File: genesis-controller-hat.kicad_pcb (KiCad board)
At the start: 2 copper layers, 65 x 56 mm, 7 parts, among them J1 GPIO, J2 DSUB-9_Socket_Horizontal_P2.7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, J3 DSUB-9_Socket_Horizontal_P2.7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

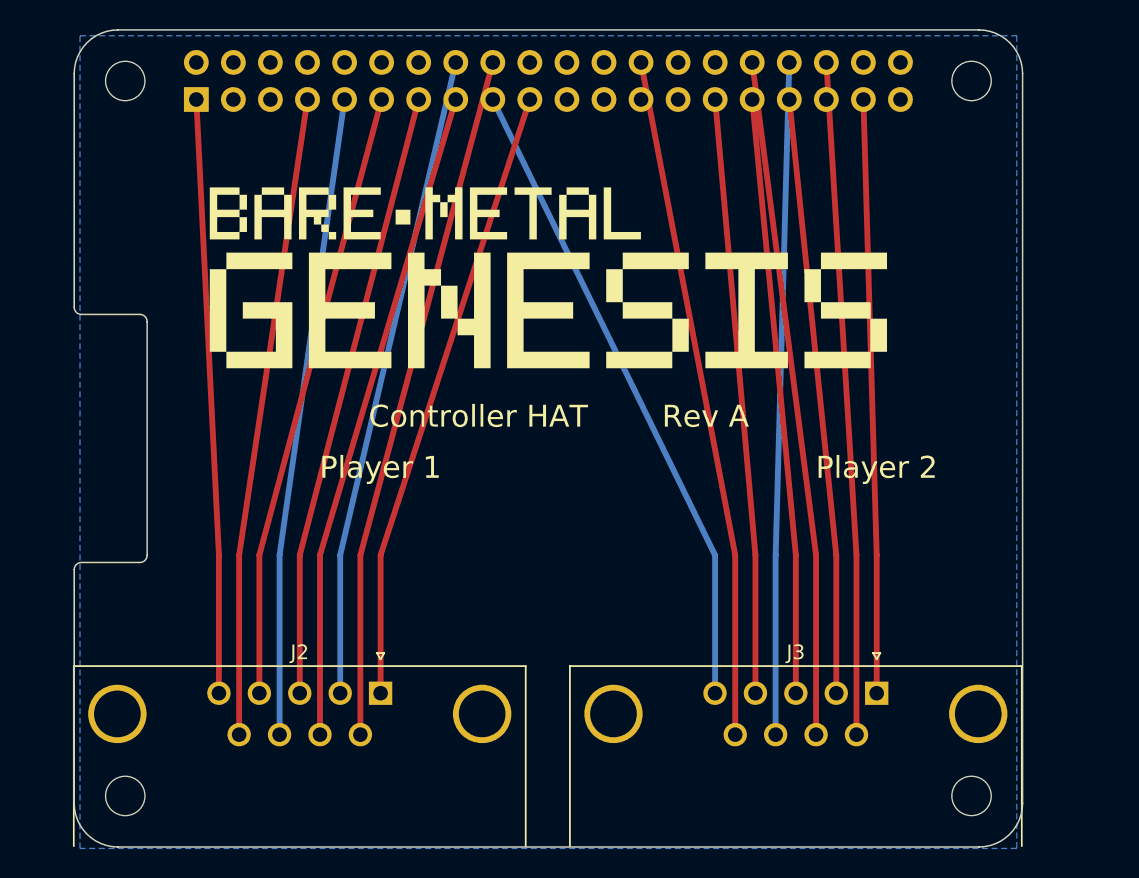
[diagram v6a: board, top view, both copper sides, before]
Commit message: Fix shorting_items and solder_mask_bridge by jogging tracks around J1's row-A pins
Root cause: J1's two pin rows are only 2.54mm apart. A track targeting a
row-B pin was routed as a straight diagonal that skimmed directly past the
row-A pin in the same column, since the diagonal has to pass through that
column's row-A position en route to row-B. Fixed by rerouting each affected
track (/GPIO24, /GPIO23, /GPIO7/SPI0.CE1, GND, /GPIO16, /GPIO12/PWM0) as:
breakout -> horizontal repositioning done entirely above J1's pin field
(y=60, clear of any pad) -> a pure-vertical run at a waypoint X exactly
between two header columns -> a short final hop into the target pad. Layer
assignment for all 12 signal nets + GND was then re-solved globally
(distance-based conflict check, not just literal intersection) to restore
zero same-layer crossings for the newly-shaped paths.

Result: shorting_items 7->0, solder_mask_bridge 6->0. Total DRC 17/5 -> 6/5.

Residual: 2 tracks_crossing remain (/GPIO12/PWM0 vs GND, /GPIO24 vs a
neighbor) in a cluster where 3+ nets mutually conflict -- more than 2
layers can pairwise-separate. This is a genuine topological limit of
2-layer routing in this specific column cluster, not a missed assignment;
resolving it needs a via or manual interactive routing, documented in
README.md as the remaining pre-fab cleanup item.

Co-Authored-By: Claude Sonnet 5 <noreply@anthropic.com>
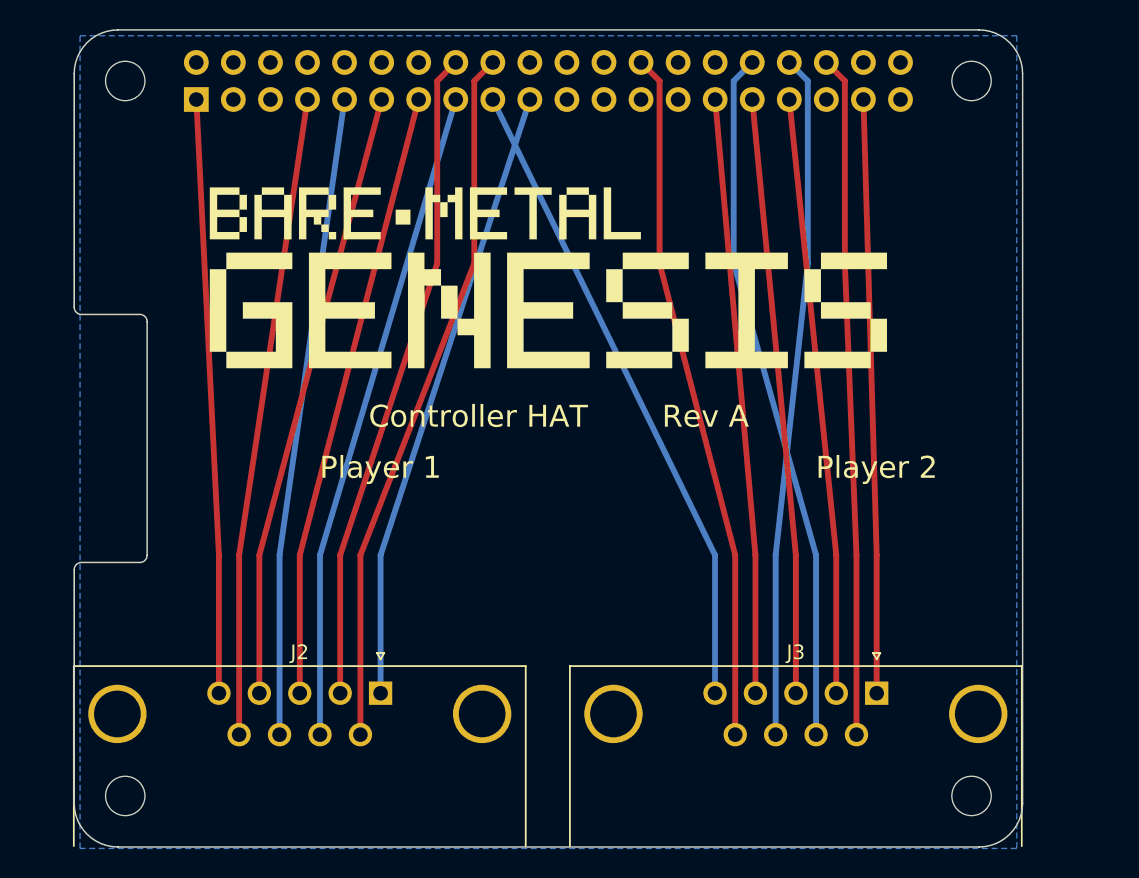
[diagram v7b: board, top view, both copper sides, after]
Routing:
- net /GPIO12/PWM0: track 46.4 -> 47.4 mm
- net /GPIO24: track 47.3 -> 48.1 mm
- net /GPIO23: track 44.1 -> 44.8 mm
- net GND: track 89.9 -> 90.6 mm
- net /GPIO7/SPI0.CE1: track 46.7 -> 47.3 mm
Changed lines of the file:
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@@
 	)
 	(segment
-		(start 153.615 80)
-		(end 151.55 46.23)
+		(start 152.82 60)
+		(end 152.82 47.5)
 		(width 0.4)
 		(layer "F.Cu")
@@
 	)
 	(segment
-		(start 150.845 80)
-		(end 146.47 46.23)
-		(width 0.4)
-		(layer "F.Cu")
+		(start 153.615 80)
+		(end 152.82 60)
+		(width 0.4)
+		(layer "F.Cu")
+		(net "/GPIO16")
+	)
+	(segment
+		(start 152.82 47.5)
+		(end 151.55 46.23)
+		(width 0.4)
+		(layer "F.Cu")
+		(net "/GPIO16")
+	)
+	(segment
+		(start 145.2 60)
+		(end 145.2 47.5)
+		(width 0.4)
+		(layer "B.Cu")
 		(net "/GPIO12{slash}PWM0")
 	)
@@
 		(end 150.845 80)
 		(width 0.4)
-		(layer "F.Cu")
-		(net "/GPIO12{slash}PWM0")
+		(layer "B.Cu")
+		(net "/GPIO12{slash}PWM0")
+	)
+	(segment
+		(start 150.845 80)
+		(end 145.2 60)
+		(width 0.4)
+		(layer "B.Cu")
+		(net "/GPIO12{slash}PWM0")
+	)
+	(segment
+		(start 145.2 47.5)
+		(end 146.47 46.23)
+		(width 0.4)
+		(layer "B.Cu")
+		(net "/GPIO12{slash}PWM0")
+	)
+	(segment
+		(start 148.075 80)
+		(end 150.28 60)
+		(width 0.4)
+		(layer "B.Cu")
+		(net "GND")
 	)
 	(segment
@@
 	)
 	(segment
-		(start 148.075 80)
-		(end 149.01 46.23)
+		(start 150.28 60)
+		(end 150.28 47.5)
 		(width 0.4)
 		(layer "B.Cu")
@@
 	)
 	(segment
+		(start 150.28 47.5)
+		(end 149.01 46.23)
+		(width 0.4)
+		(layer "B.Cu")
+		(net "GND")
+	)
+	(segment
 		(start 145.305 80)
+		(end 140.12 60)
+		(width 0.4)
+		(layer "F.Cu")
+		(net "/GPIO7{slash}SPI0.CE1")
+	)
+	(segment
+		(start 140.12 47.5)
 		(end 138.85 46.23)
+		(width 0.4)
+		(layer "F.Cu")
+		(net "/GPIO7{slash}SPI0.CE1")
+	)
+	(segment
+		(start 140.12 60)
+		(end 140.12 47.5)
 		(width 0.4)
 		(layer "F.Cu")
@@
 		(end 121 80)
 		(width 0.4)
-		(layer "F.Cu")
+		(layer "B.Cu")
 		(net "/GPIO10{slash}SPI0.MOSI")
 	)
@@
 		(end 131.23 48.77)
 		(width 0.4)
-		(layer "F.Cu")
+		(layer "B.Cu")
 		(net "/GPIO10{slash}SPI0.MOSI")
 	)
 	(segment
+		(start 124.88 47.5)
+		(end 126.15 46.23)
+		(width 0.4)
+		(layer "F.Cu")
+		(net "/GPIO23")
+	)
+	(segment
 		(start 118.23 80)
-		(end 126.15 46.23)
-		(width 0.4)
-		(layer "B.Cu")
+		(end 124.88 60)
+		(width 0.4)
+		(layer "F.Cu")
+		(net "/GPIO23")
+	)
+	(segment
+		(start 124.88 60)
+		(end 124.88 47.5)
+		(width 0.4)
+		(layer "F.Cu")
 		(net "/GPIO23")
 	)
@@
 		(end 118.23 80)
 		(width 0.4)
-		(layer "B.Cu")
+		(layer "F.Cu")
 		(net "/GPIO23")
 	)
@@
 	)
 	(segment
-		(start 119.615 80)
+		(start 127.42 60)
+		(end 127.42 47.5)
+		(width 0.4)
+		(layer "F.Cu")
+		(net "/GPIO24")
+	)
+	(segment
+		(start 127.42 47.5)
 		(end 128.69 46.23)
 		(width 0.4)
@@
 	)
 	(segment
+		(start 119.615 80)
+		(end 127.42 60)
+		(width 0.4)
+		(layer "F.Cu")
+		(net "/GPIO24")
+	)
+	(segment
 		(start 116.845 80)
 		(end 126.15 48.77)
 		(width 0.4)
-		(layer "F.Cu")
+		(layer "B.Cu")
 		(net "/GPIO22")
 	)
@@
 		(end 116.845 80)
 		(width 0.4)
-		(layer "F.Cu")
+		(layer "B.Cu")
 		(net "/GPIO22")
 	)

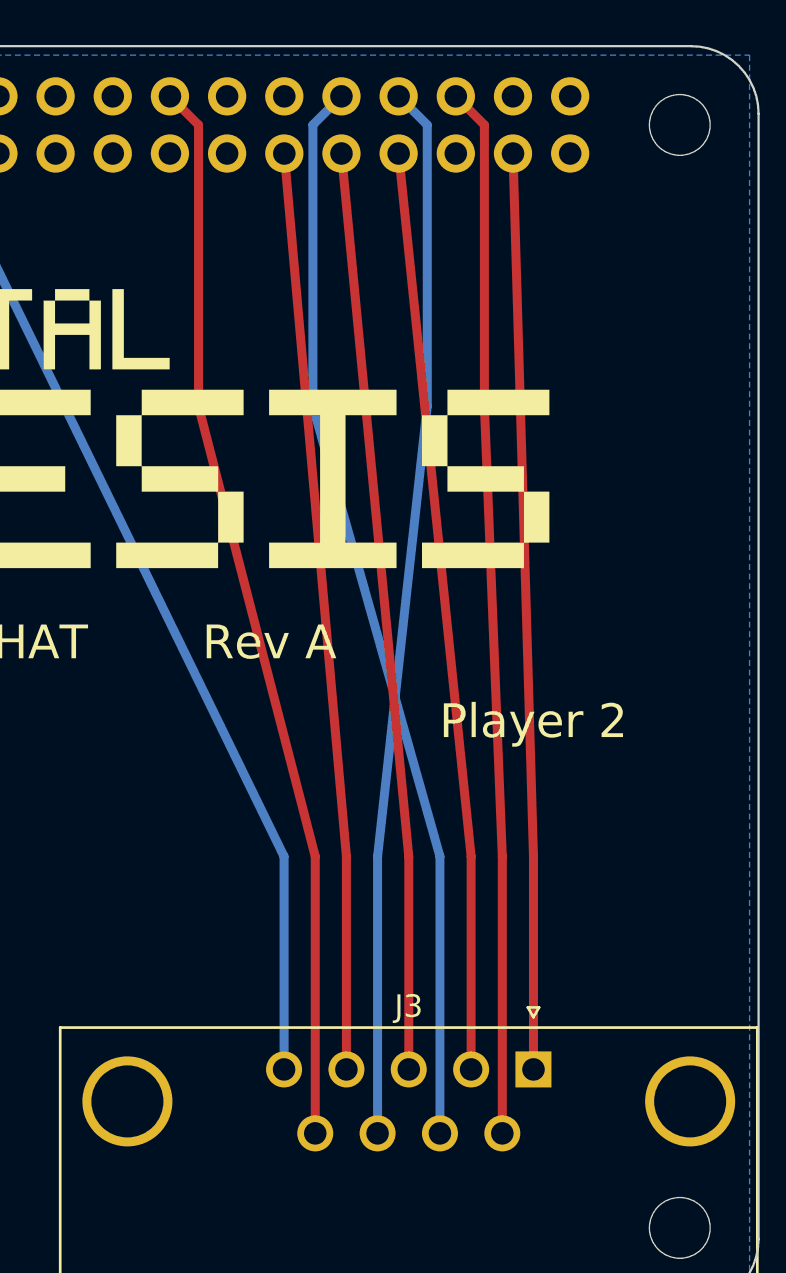
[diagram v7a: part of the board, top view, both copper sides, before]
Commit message: Resolve GPIO12/PWM0-vs-GND crossing; incorporate manual GPIO6 reroute
Builds on a manual reroute of /GPIO6 further left (clearing space around
x=147.74), which opened room for /GPIO12/PWM0 to approach its target (J1
pin 32) from the opposite side of the pin, on F.Cu -- parallel to /GPIO6
instead of crossing GND on B.Cu. This was tried once before this session
without the /GPIO6 reroute and made things worse (new shorting_items
against /GPIO6, since the two ran too close together); with /GPIO6 moved
out of the way first, it now resolves cleanly with no new violations.

tracks_crossing: 2 -> 1 (only /GPIO24 vs /GPIO10/SPI0.MOSI/+3V3 remains,
a separate three-way layer conflict). Total DRC: 6 errors/5 warnings ->
5/5. ERC and check_pinmap.py unaffected.

Co-Authored-By: Claude Sonnet 5 <noreply@anthropic.com>
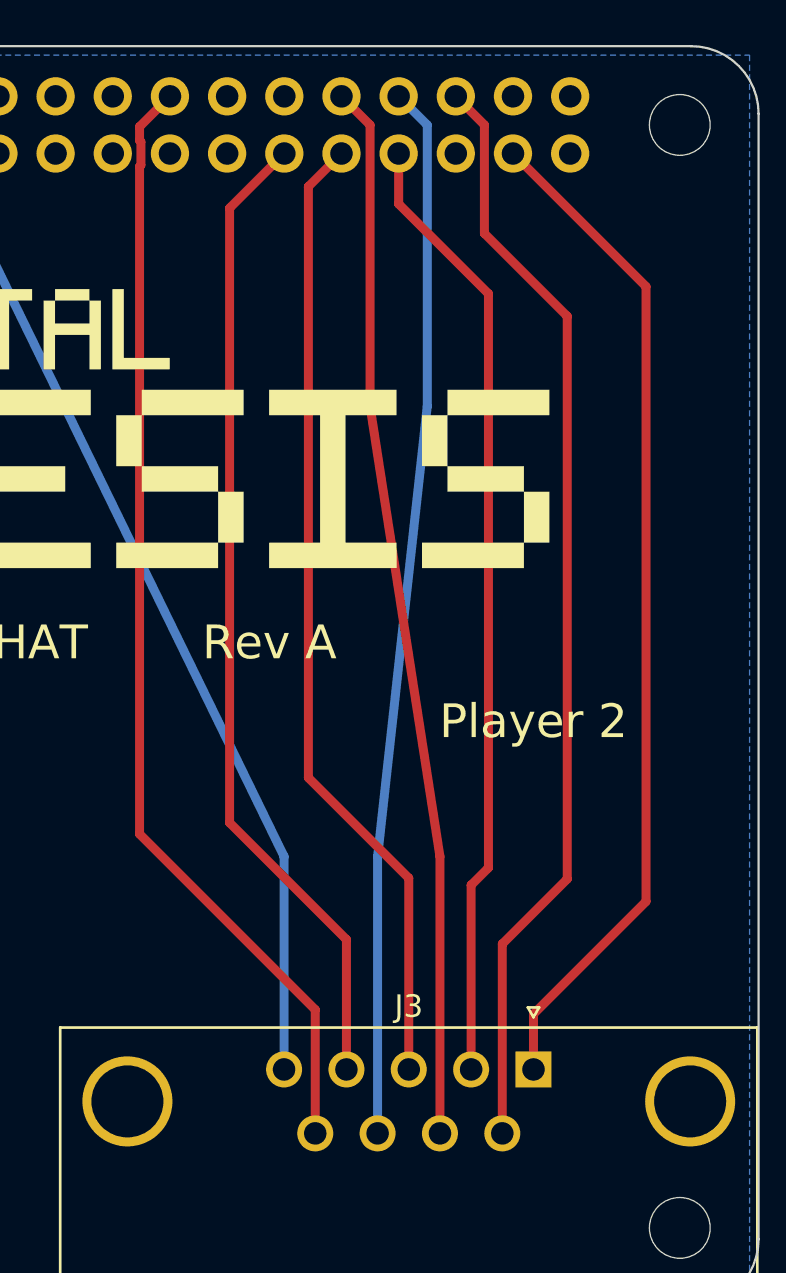
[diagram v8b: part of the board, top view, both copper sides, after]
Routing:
- net /GPIO26: track 40.7 -> 45.2 mm
- net /GPIO5: track 40.8 -> 43.8 mm
- net /GPIO16: track 46.6 -> 49.3 mm
- net /GPIO7/SPI0.CE1: track 47.3 -> 49.9 mm
- net /GPIO6: track 40.8 -> 43.1 mm
- net /GPIO13/PWM1: track 40.9 -> 42.7 mm
- net /GPIO12/PWM0: track 47.4 -> 46.8 mm
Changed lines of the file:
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@@
 		)
 		(embedded_fonts no)
-		(model "${KICAD9_3DMODEL_DIR}/Connector_PinSocket_2.54mm.3dshapes/PinSocket_2x20_P2.54mm_Vertical.wrl"
+		(model "${KICAD9_3DMODEL_DIR}/Connector_PinSocket_2.54mm.3dshapes/PinSocket_2x20_P2.54mm_Vertical.step"
 			(offset
 				(xyz 0 0 0)
@@
 	)
 	(segment
+		(start 160 54.68)
+		(end 154.09 48.77)
+		(width 0.4)
+		(layer "F.Cu")
+		(net "/GPIO26")
+	)
+	(segment
+		(start 160 82)
+		(end 160 54.68)
+		(width 0.4)
+		(layer "F.Cu")
+		(net "/GPIO26")
+	)
+	(segment
 		(start 155 89.46)
-		(end 155 80)
+		(end 155 87)
 		(width 0.4)
 		(layer "F.Cu")
@@
 	)
 	(segment
-		(start 155 80)
-		(end 154.09 48.77)
+		(start 155 87)
+		(end 160 82)
 		(width 0.4)
 		(layer "F.Cu")
@@
 	)
 	(segment
+		(start 149.01 51.01)
+		(end 149.01 48.77)
+		(width 0.4)
+		(layer "F.Cu")
+		(net "/GPIO13{slash}PWM1")
+	)
+	(segment
+		(start 153 55)
+		(end 149.01 51.01)
+		(width 0.4)
+		(layer "F.Cu")
+		(net "/GPIO13{slash}PWM1")
+	)
+	(segment
+		(start 152.23 81.27)
+		(end 153 80.5)
+		(width 0.4)
+		(layer "F.Cu")
+		(net "/GPIO13{slash}PWM1")
+	)
+	(segment
 		(start 152.23 89.46)
-		(end 152.23 80)
+		(end 152.23 81.27)
 		(width 0.4)
 		(layer "F.Cu")
@@
 	)
 	(segment
-		(start 152.23 80)
-		(end 149.01 48.77)
+		(start 153 80.5)
+		(end 153 55)
 		(width 0.4)
 		(layer "F.Cu")
@@
 	)
 	(segment
-		(start 149.46 80)
+		(start 149.46 89.46)
+		(end 149.46 80.96)
+		(width 0.4)
+		(layer "F.Cu")
+		(net "/GPIO6")
+	)
+	(segment
+		(start 149.46 80.96)
+		(end 145 76.5)
+		(width 0.4)
+		(layer "F.Cu")
+		(net "/GPIO6")
+	)
+	(segment
+		(start 145 76.5)
+		(end 145 50.24)
+		(width 0.4)
+		(layer "F.Cu")
+		(net "/GPIO6")
+	)
+	(segment
+		(start 145 50.24)
 		(end 146.47 48.77)
 		(width 0.4)
@@
 	)
 	(segment
-		(start 149.46 89.46)
-		(end 149.46 80)
-		(width 0.4)
-		(layer "F.Cu")
-		(net "/GPIO6")
-	)
-	(segment
-		(start 146.69 80)
+		(start 141.5 78.5)
+		(end 141.5 51.2)
+		(width 0.4)
+		(layer "F.Cu")
+		(net "/GPIO5")
+	)
+	(segment
+		(start 141.5 51.2)
 		(end 143.93 48.77)
 		(width 0.4)
@@
 	)
 	(segment
+		(start 146.69 83.69)
+		(end 141.5 78.5)
+		(width 0.4)
+		(layer "F.Cu")
+		(net "/GPIO5")
+	)
+	(segment
 		(start 146.69 89.46)
-		(end 146.69 80)
+		(end 146.69 83.69)
 		(width 0.4)
 		(layer "F.Cu")
@@
 	)
 	(segment
-		(start 152.82 60)
+		(start 156.5 56)
+		(end 152.82 52.32)
+		(width 0.4)
+		(layer "F.Cu")
+		(net "/GPIO16")
+	)
+	(segment
+		(start 153.615 83.885)
+		(end 156.5 81)
+		(width 0.4)
+		(layer "F.Cu")
+		(net "/GPIO16")
+	)
+	(segment
+		(start 153.615 92.3)
+		(end 153.615 83.885)
+		(width 0.4)
+		(layer "F.Cu")
+		(net "/GPIO16")
+	)
+	(segment
+		(start 152.82 52.32)
 		(end 152.82 47.5)
 		(width 0.4)
@@
 	)
 	(segment
-		(start 153.615 92.3)
-		(end 153.615 80)
-		(width 0.4)
-		(layer "F.Cu")
-		(net "/GPIO16")
-	)
-	(segment
-		(start 153.615 80)
-		(end 152.82 60)
+		(start 156.5 81)
+		(end 156.5 56)
 		(width 0.4)
 		(layer "F.Cu")
@@
 	)
 	(segment
-		(start 145.2 60)
-		(end 145.2 47.5)
-		(width 0.4)
-		(layer "B.Cu")
+		(start 147.74 60)
+		(end 147.74 47.5)
+		(width 0.4)
+		(layer "F.Cu")
+		(net "/GPIO12{slash}PWM0")
+	)
+	(segment
+		(start 147.74 47.5)
+		(end 146.47 46.23)
+		(width 0.4)
+		(layer "F.Cu")
+		(net "/GPIO12{slash}PWM0")
+	)
+	(segment
+		(start 150.845 80)
+		(end 147.74 60)
+		(width 0.4)
+		(layer "F.Cu")
 		(net "/GPIO12{slash}PWM0")
 	)
@@
 		(end 150.845 80)
 		(width 0.4)
-		(layer "B.Cu")
-		(net "/GPIO12{slash}PWM0")
-	)
-	(segment
-		(start 150.845 80)
-		(end 145.2 60)
-		(width 0.4)
-		(layer "B.Cu")
-		(net "/GPIO12{slash}PWM0")
-	)
-	(segment
-		(start 145.2 47.5)
-		(end 146.47 46.23)
-		(width 0.4)
-		(layer "B.Cu")
+		(layer "F.Cu")
 		(net "/GPIO12{slash}PWM0")
 	)
@@
 	)
 	(segment
-		(start 145.305 80)
-		(end 140.12 60)
+		(start 137.56 49.287767)
+		(end 137.56 48.252233)
 		(width 0.4)
 		(layer "F.Cu")
@@
 	)
 	(segment
-		(start 140.12 47.5)
+		(start 137.5 79)
+		(end 137.5 49.347767)
+		(width 0.4)
+		(layer "F.Cu")
+		(net "/GPIO7{slash}SPI0.CE1")
+	)
+	(segment
+		(start 137.56 48.252233)
+		(end 137.5 48.192233)
+		(width 0.4)
+		(layer "F.Cu")
+		(net "/GPIO7{slash}SPI0.CE1")
+	)
+	(segment
+		(start 145.305 86.805)
+		(end 137.5 79)
+		(width 0.4)
+		(layer "F.Cu")
+		(net "/GPIO7{slash}SPI0.CE1")
+	)
+	(segment
+		(start 137.5 48.192233)
+		(end 137.5 47.58)
+		(width 0.4)
+		(layer "F.Cu")
+		(net "/GPIO7{slash}SPI0.CE1")
+	)
+	(segment
+		(start 137.5 47.58)
 		(end 138.85 46.23)
 		(width 0.4)
@@
 	)
 	(segment
-		(start 140.12 60)
-		(end 140.12 47.5)
+		(start 137.5 49.347767)
+		(end 137.56 49.287767)
 		(width 0.4)
 		(layer "F.Cu")
@@
 	(segment
 		(start 145.305 92.3)
-		(end 145.305 80)
-		(width 0.4)
-		(layer "F.Cu")
+		(end 145.305 86.805)
+		(width 0.4)
+		(layer "F.Cu")
